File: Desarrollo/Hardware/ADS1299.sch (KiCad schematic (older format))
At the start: 32 parts, among them J2 IOs Multipropósito, U10 ADS1299, U14 OPA2376

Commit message: Actualización de PCB. Cotas de diseño. Generación de BOM. Archivos Gerber disponibles en carpeta "gerbers". Colocación de eje auxiliar de posicionamiento en mounting hole inferior izquierdo. Actualización de esquemático con modificación de comentarios y adición de código de compra DigiKey y hoja de datos en algunos componentes que faltaban. FINALIZADO
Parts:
- C19, C24, C26, C28: Código Digikey (none) -> 399-1170-1-ND
- C20: Código Digikey (none) -> 399-8012-1-ND
- C21, C23, C25, C27, C29, C36, C37, C39, C40: Código Digikey (none) -> 399-1284-1-ND
- C22: Código Digikey (none) -> 399-11631-1-ND
- C35: Código Digikey (none) -> 399-1158-1-ND
- C38: Código Digikey (none) -> 399-1147-1-ND
- J2, JP1, JP2, JP3, JP4: Código Digikey (none) -> 3M9455-ND
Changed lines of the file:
@@
 F 2 "Capacitors_SMD:C_0805" H 2938 4400 50  0001 C CNN
 F 3 "http://www.kemet.com/Lists/ProductCatalog/Attachments/53/KEM_C1002_X7R_SMD.pdf" H 2900 4550 50  0001 C CNN
+F 4 "399-1170-1-ND" H 2900 4550 60  0001 C CNN "Código Digikey"
 	1    2900 4550
 	1    0    0    -1
@@
 F 2 "Capacitors_SMD:C_0805" H 3138 4400 50  0001 C CNN
 F 3 "http://www.kemet.com/Lists/ProductCatalog/Attachments/19/KEM_C1006_X5R_SMD.pdf" H 3100 4550 50  0001 C CNN
+F 4 "399-8012-1-ND" H 3100 4550 60  0001 C CNN "Código Digikey"
 	1    3100 4550
 	1    0    0    -1
@@
 F 2 "Capacitors_SMD:C_0805" H 3438 5100 50  0001 C CNN
 F 3 "http://www.kemet.com/Lists/ProductCatalog/Attachments/53/KEM_C1002_X7R_SMD.pdf" H 3400 5250 50  0001 C CNN
+F 4 "399-1284-1-ND" H 3400 5250 60  0001 C CNN "Código Digikey"
 	1    3400 5250
 	-1   0    0    -1
@@
 F 2 "Capacitors_SMD:C_0805" H 3938 5100 50  0001 C CNN
 F 3 "http://www.kemet.com/Lists/ProductCatalog/Attachments/53/KEM_C1002_X7R_SMD.pdf" H 3900 5250 50  0001 C CNN
+F 4 "399-1284-1-ND" H 3900 5250 60  0001 C CNN "Código Digikey"
 	1    3900 5250
 	1    0    0    -1
@@
 F 2 "Capacitors_SMD:C_1206" H 3638 5100 50  0001 C CNN
 F 3 "http://www.kemet.com/Lists/ProductCatalog/Attachments/19/KEM_C1006_X5R_SMD.pdf" H 3600 5250 50  0001 C CNN
+F 4 "399-11631-1-ND" H 3600 5250 60  0001 C CNN "Código Digikey"
 	1    3600 5250
 	1    0    0    -1
@@
 F 2 "Capacitors_SMD:C_0805" H 7638 3200 50  0001 C CNN
 F 3 "http://www.kemet.com/Lists/ProductCatalog/Attachments/53/KEM_C1002_X7R_SMD.pdf" H 7600 3350 50  0001 C CNN
+F 4 "399-1170-1-ND" H 7600 3350 60  0001 C CNN "Código Digikey"
 	1    7600 3350
 	1    0    0    -1
@@
 F 2 "Capacitors_SMD:C_0805" H 7938 3200 50  0001 C CNN
 F 3 "http://www.kemet.com/Lists/ProductCatalog/Attachments/53/KEM_C1002_X7R_SMD.pdf" H 7900 3350 50  0001 C CNN
+F 4 "399-1284-1-ND" H 7900 3350 60  0001 C CNN "Código Digikey"
 	1    7900 3350
 	1    0    0    -1
@@
 F 2 "Capacitors_SMD:C_0805" H 8838 2250 50  0001 C CNN
 F 3 "http://www.kemet.com/Lists/ProductCatalog/Attachments/53/KEM_C1002_X7R_SMD.pdf" H 8800 2400 50  0001 C CNN
+F 4 "399-1170-1-ND" H 8800 2400 60  0001 C CNN "Código Digikey"
 	1    8800 2400
 	1    0    0    -1
@@
 F 2 "Capacitors_SMD:C_0805" H 9238 2250 50  0001 C CNN
 F 3 "http://www.kemet.com/Lists/ProductCatalog/Attachments/53/KEM_C1002_X7R_SMD.pdf" H 9200 2400 50  0001 C CNN
+F 4 "399-1284-1-ND" H 9200 2400 60  0001 C CNN "Código Digikey"
 	1    9200 2400
 	1    0    0    -1
@@
 F 2 "Capacitors_SMD:C_0805" H 9738 2250 50  0001 C CNN
 F 3 "http://www.kemet.com/Lists/ProductCatalog/Attachments/53/KEM_C1002_X7R_SMD.pdf" H 9700 2400 50  0001 C CNN
+F 4 "399-1170-1-ND" H 9700 2400 60  0001 C CNN "Código Digikey"
 	1    9700 2400
 	1    0    0    -1
@@
 F 2 "Capacitors_SMD:C_0805" H 10138 2250 50  0001 C CNN
 F 3 "http://www.kemet.com/Lists/ProductCatalog/Attachments/53/KEM_C1002_X7R_SMD.pdf" H 10100 2400 50  0001 C CNN
+F 4 "399-1284-1-ND" H 10100 2400 60  0001 C CNN "Código Digikey"
 	1    10100 2400
 	1    0    0    -1
@@
 F 2 "Capacitors_SMD:C_0805" H 5738 1650 50  0001 C CNN
 F 3 "http://www.kemet.com/Lists/ProductCatalog/Attachments/53/KEM_C1002_X7R_SMD.pdf" H 5700 1800 50  0001 C CNN
+F 4 "399-1158-1-ND" H 5700 1800 60  0001 C CNN "Código Digikey"
 	1    5700 1800
 	1    0    0    -1
@@
 F 1 "JUMPER" H 4750 1070 50  0000 C CNN
 F 2 "Pin_Headers:Pin_Header_Straight_1x02" H 4750 1150 50  0001 C CNN
-F 3 "" H 4750 1150 50  0000 C CNN
+F 3 "http://multimedia.3m.com/mws/media/548112O/3mtm-pin-strip-header-ts2181.pdf" H 4750 1150 50  0001 C CNN
+F 4 "3M9455-ND" H 4750 1150 60  0001 C CNN "Código Digikey"
 	1    4750 1150
 	1    0    0    -1
@@
 F 1 "JUMPER3" H 5550 1400 50  0000 C BNN
 F 2 "Pin_Headers:Pin_Header_Straight_1x03" H 5550 1300 50  0001 C CNN
-F 3 "" H 5550 1300 50  0000 C CNN
+F 3 "http://multimedia.3m.com/mws/media/548112O/3mtm-pin-strip-header-ts2181.pdf" H 5550 1300 50  0001 C CNN
+F 4 "3M9455-ND" H 5550 1300 60  0001 C CNN "Código Digikey"
 	1    5550 1300
 	1    0    0    -1
@@
 F 2 "Capacitors_SMD:C_0805" H 3338 600 50  0001 C CNN
 F 3 "http://www.kemet.com/Lists/ProductCatalog/Attachments/53/KEM_C1002_X7R_SMD.pdf" H 3300 750 50  0001 C CNN
+F 4 "399-1284-1-ND" H 3300 750 60  0001 C CNN "Código Digikey"
 	1    3300 750
 	0    1    1    0
@@
 F 2 "Capacitors_SMD:C_0805" H 3338 1600 50  0001 C CNN
 F 3 "http://www.kemet.com/Lists/ProductCatalog/Attachments/53/KEM_C1002_X7R_SMD.pdf" H 3300 1750 50  0001 C CNN
+F 4 "399-1284-1-ND" H 3300 1750 60  0001 C CNN "Código Digikey"
 	1    3300 1750
 	0    1    1    0
@@
 F 1 "JUMPER3" H 2400 3900 50  0000 C BNN
 F 2 "Pin_Headers:Pin_Header_Straight_1x03" H 2400 3800 50  0001 C CNN
-F 3 "" H 2400 3800 50  0000 C CNN
+F 3 "http://multimedia.3m.com/mws/media/548112O/3mtm-pin-strip-header-ts2181.pdf" H 2400 3800 50  0001 C CNN
+F 4 "3M9455-ND" H 2400 3800 60  0001 C CNN "Código Digikey"
 	1    2400 3800
 	0    -1   -1   0
@@
 F 2 "Capacitors_SMD:C_0805" H 3588 3950 50  0001 C CNN
 F 3 "http://www.kemet.com/Lists/ProductCatalog/Attachments/53/KEM_C1002_X7R_SMD.pdf" H 3550 4100 50  0001 C CNN
+F 4 "399-1147-1-ND" H 3550 4100 60  0001 C CNN "Código Digikey"
 	1    3550 4100
 	0    -1   -1   0
@@
 F 1 "JUMPER3" H 850 4250 50  0000 C BNN
 F 2 "Pin_Headers:Pin_Header_Straight_1x03" H 850 4150 50  0001 C CNN
-F 3 "" H 850 4150 50  0000 C CNN
+F 3 "http://multimedia.3m.com/mws/media/548112O/3mtm-pin-strip-header-ts2181.pdf" H 850 4150 50  0001 C CNN
+F 4 "3M9455-ND" H 850 4150 60  0001 C CNN "Código Digikey"
 	1    850  4150
 	0    -1   -1   0
@@
 F 2 "Capacitors_SMD:C_0805" H 1388 3600 50  0001 C CNN
 F 3 "http://www.kemet.com/Lists/ProductCatalog/Attachments/53/KEM_C1002_X7R_SMD.pdf" H 1350 3750 50  0001 C CNN
+F 4 "399-1284-1-ND" H 1350 3750 60  0001 C CNN "Código Digikey"
 	1    1350 3750
 	0    1    1    0
@@
 F 2 "Capacitors_SMD:C_0805" H 1388 4600 50  0001 C CNN
 F 3 "http://www.kemet.com/Lists/ProductCatalog/Attachments/53/KEM_C1002_X7R_SMD.pdf" H 1350 4750 50  0001 C CNN
+F 4 "399-1284-1-ND" H 1350 4750 60  0001 C CNN "Código Digikey"
 	1    1350 4750
 	0    1    1    0
@@
 F 1 "IOs Multipropósito" V 8850 3600 50  0000 C CNN
 F 2 "Pin_Headers:Pin_Header_Straight_1x05" H 8750 3600 50  0001 C CNN
-F 3 "" H 8750 3600 50  0000 C CNN
+F 3 "http://multimedia.3m.com/mws/media/548112O/3mtm-pin-strip-header-ts2181.pdf" H 8750 3600 50  0001 C CNN
+F 4 "3M9455-ND" H 8750 3600 60  0001 C CNN "Código Digikey"
 	1    8750 3600
 	1    0    0    -1
@@
 F 1 "J_STD" H 1300 6813 60  0001 C CNN
 F 2 "footprints:Jumpers_Default" H 1300 6400 60  0001 C CNN
-F 3 "" H 1300 6400 60  0000 C CNN
+F 3 "NONE" H 1300 6400 60  0001 C CNN
 	1    1300 6400
 	1    0    0    -1
@@
 F 1 "J_CFG" H 2550 7770 60  0001 C CNN
 F 2 "footprints:Jumpers_Default" H 2550 6850 60  0001 C CNN
-F 3 "" H 2550 6850 60  0000 C CNN
+F 3 "NONE" H 2550 6850 60  0001 C CNN
 	1    2550 6850
 	1    0    0    -1

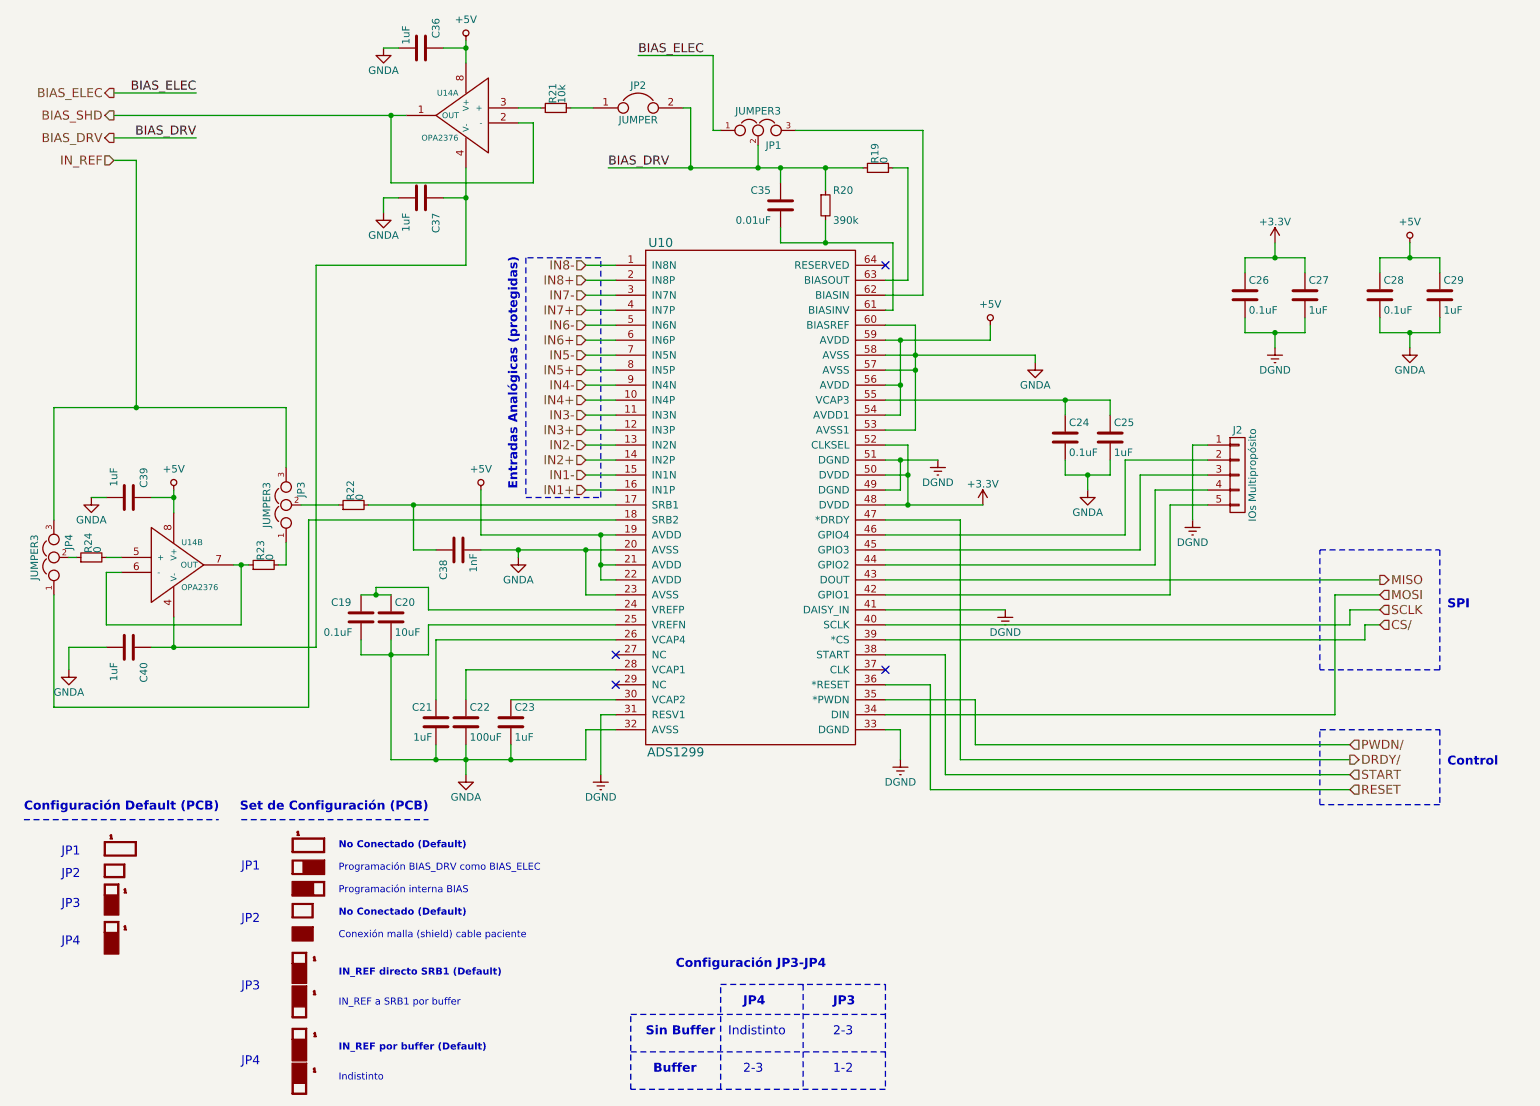
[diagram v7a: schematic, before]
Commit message: - Actualización última versión de Firmware poncho biopotenciales. - Actualización librerías, footprints y otros en Hardware poncho biopotenciales.
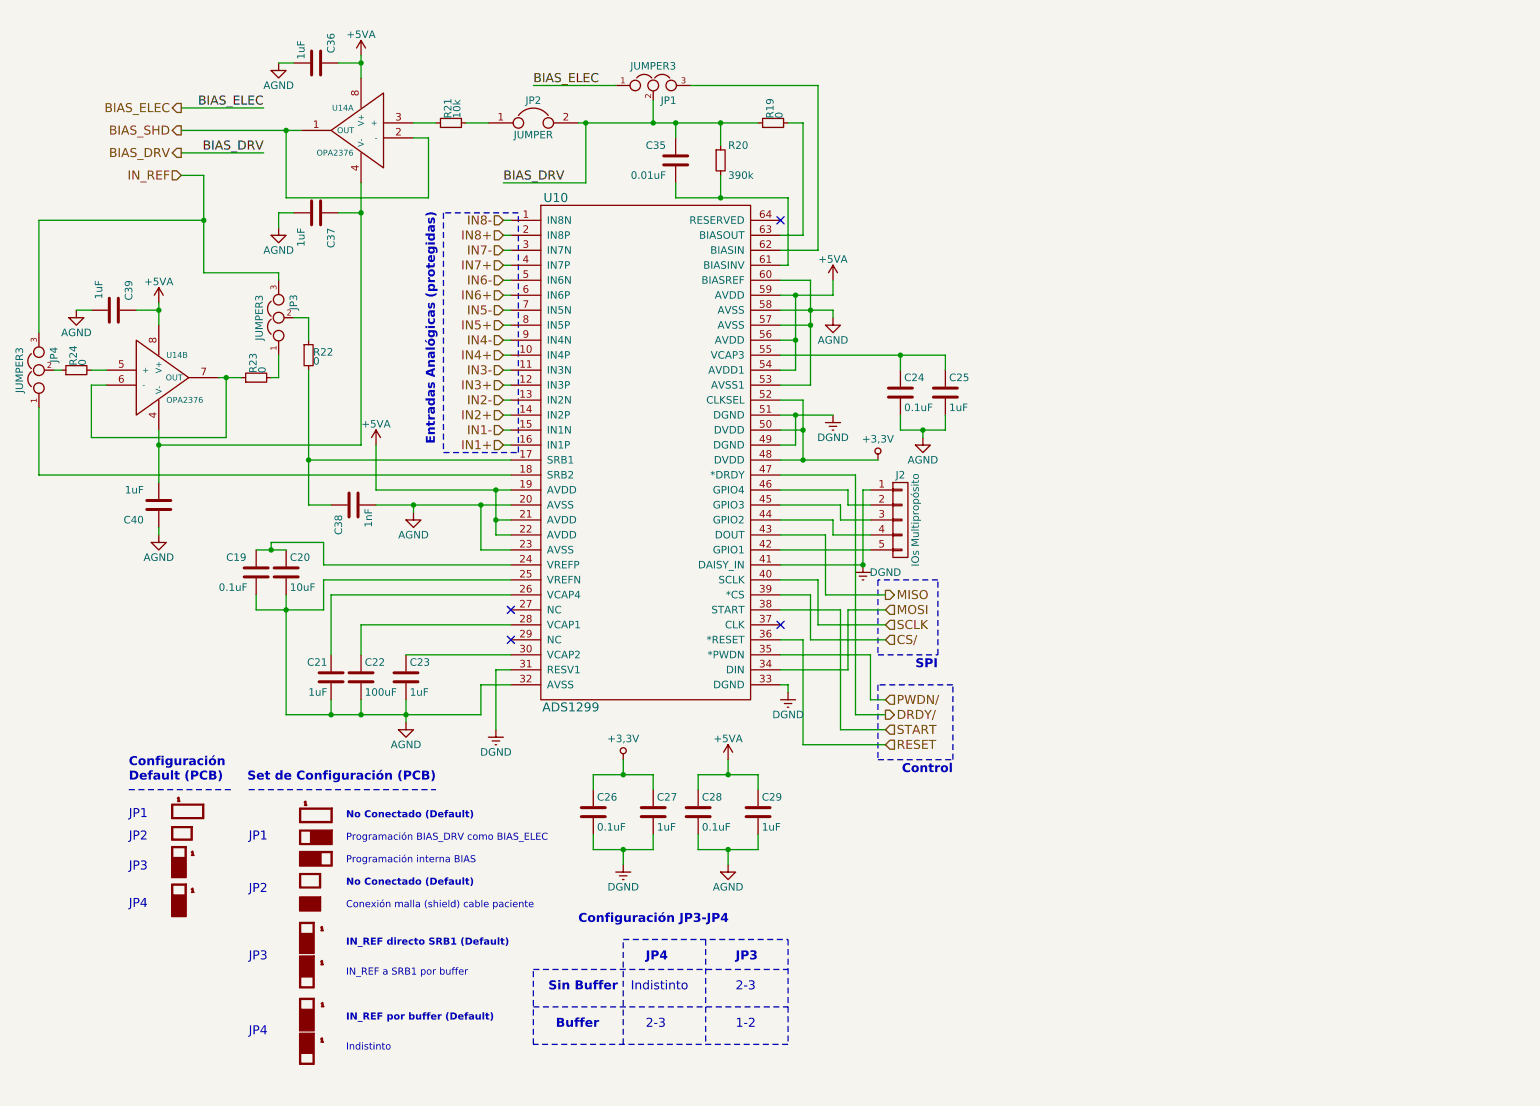
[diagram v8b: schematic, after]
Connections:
- net GNDA: now also C40.1; no longer C40.2
- net at C37.1, U14.4 (V-), U14.4 (V-): now also C40.2; no longer C40.1
- net +3V3 renamed +3.3V
- net +5V renamed +5VA
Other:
- note added: "Configuración\nDefault (PCB)"
- note removed: "Configuración Default (PCB)"
- moved on the sheet: C19, C20, C21, C22, C23, C24, C25, C26, C27, C28, C29, C35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
